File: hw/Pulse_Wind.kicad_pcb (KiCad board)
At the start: 2 copper layers, 14 x 21 mm, 22 parts, among them J1 AudioJack4, J2 Conn_01x04, U1 PY32F003F18U6, U2 SC7A20, U3 FM8002A, U4 ME6206A33XG

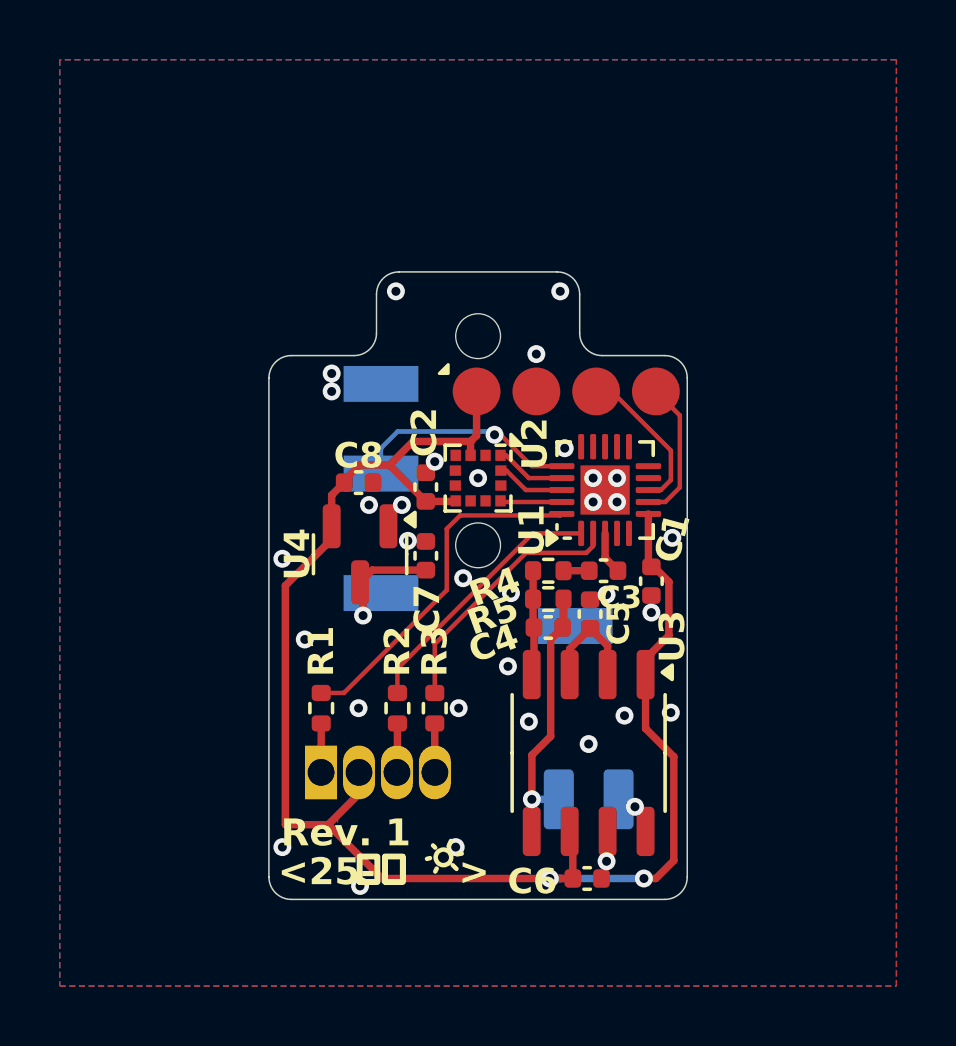
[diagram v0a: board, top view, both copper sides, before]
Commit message: hw: Fix errors (> <)
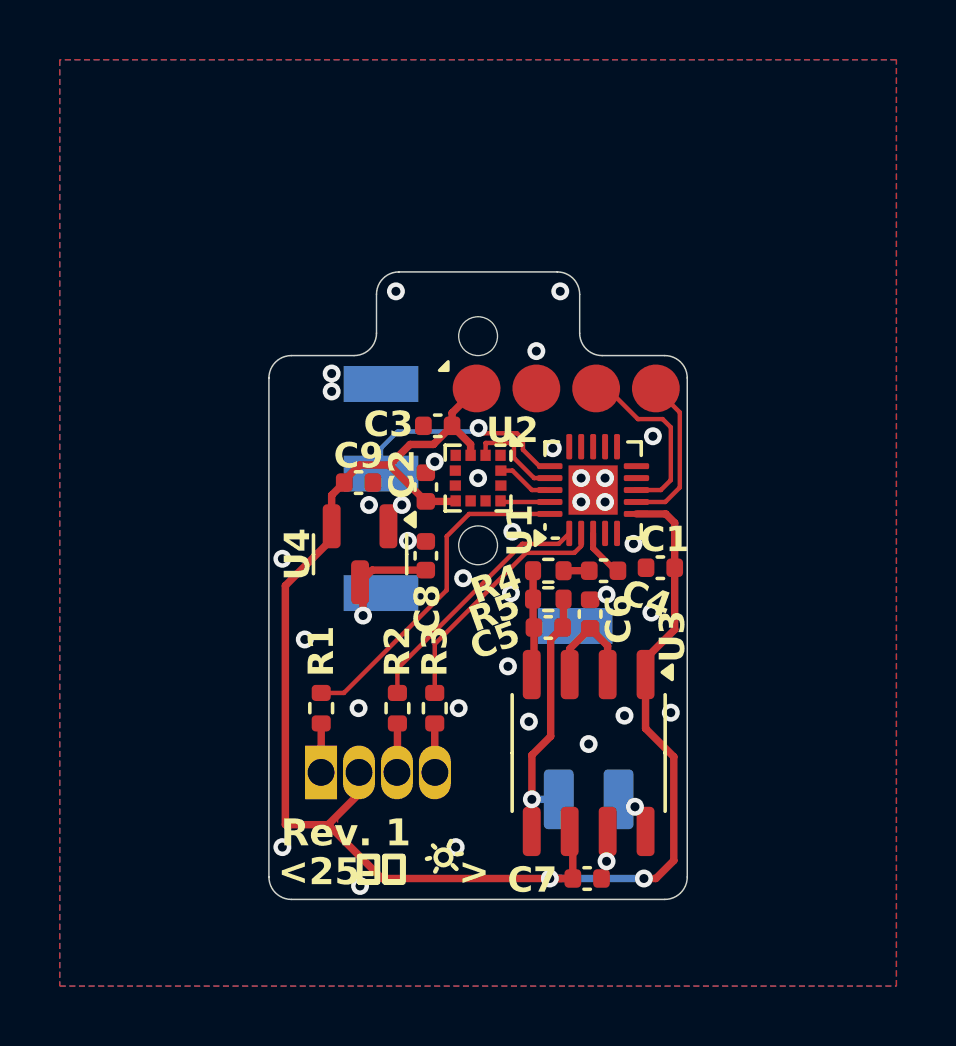
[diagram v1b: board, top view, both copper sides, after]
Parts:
- added C3: 100n, Capacitor_SMD:C_0402_1005Metric, F.Cu at (78.7, 78.2)
- moved C1 0.54 mm to (86.1, 83.0), turned to 0 degrees
- moved U1 0.40 mm to (83.8, 80.4)
- moved J2 0.10 mm to (83.0, 77.0)
- renumbered C3 to C4, C4 to C5, C5 to C6, C6 to C7, C7 to C8, C8 to C9
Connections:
- U2 pad 1: /IMU_SDA -> unconnected-(U2-SDO-Pad1)
- U2 pad 2: unconnected-(U2-SDx-Pad2) -> /IMU_SDA
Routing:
- net +3V3: track 53.7 -> 54.7 mm
- net /SWCLK: track 5.20 -> 6.19 mm
- net /IMU_SDA: track 2.37 -> 3.24 mm
- net /SWDIO: track 4.80 -> 5.40 mm
- net /LED_R: track 11.7 -> 11.2 mm
- net /IMU_SCK: track 2.31 -> 1.81 mm
- net GND: vias 33 -> 35

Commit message: hw: Connect SC7A20 NC (pin 4) to GND?
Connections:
- U2 pad 4: unconnected-(U2-NC-Pad4) -> GND
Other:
- board text added: "Rev. 1a"
- board text removed: "Rev. 1"
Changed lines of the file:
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@@
 	(net 32 "unconnected-(U2-INT2-Pad6)")
 	(net 33 "unconnected-(U2-INT1-Pad5)")
-	(net 34 "unconnected-(U2-NC-Pad4)")
-	(net 35 "unconnected-(U2-SDO-Pad1)")
+	(net 34 "unconnected-(U2-SDO-Pad1)")
 	(footprint "Capacitor_SMD:C_0402_1005Metric"
 		(layer "F.Cu")
@@
 			(size 0.375 0.35)
 			(layers "F.Cu" "F.Mask" "F.Paste")
-			(net 35 "unconnected-(U2-SDO-Pad1)")
+			(net 34 "unconnected-(U2-SDO-Pad1)")
 			(pinfunction "SDO")
 			(pintype "bidirectional+no_connect")
@@
 			(size 0.375 0.35)
 			(layers "F.Cu" "F.Mask" "F.Paste")
-			(net 34 "unconnected-(U2-NC-Pad4)")
+			(net 2 "GND")
 			(pinfunction "NC")
-			(pintype "passive+no_connect")
+			(pintype "passive")
 		)
 		(pad "5" smd rect
@@
 		)
 	)
-	(gr_text "Rev. 1"
+	(gr_text "Rev. 1a"
 		(at 73.4 92.4 0)
 		(layer "F.SilkS")
@@
 			(justify left bottom)
 		)
-		(render_cache "Rev. 1" 0
+		(render_cache "Rev. 1a" 0
 			(polygon
 				(pts
@@
 				)
 			)
+			(polygon
+				(pts
+					(xy 77.093753 91.625692) (xy 77.156814 91.641513) (xy 77.207073 91.667072) (xy 77.246516 91.702132)
+					(xy 77.262657 91.723709) (xy 77.276069 91.747732) (xy 77.287187 91.775525) (xy 77.295269 91.805943)
+					(xy 77.300519 91.841223) (xy 77.302274 91.879408) (xy 77.302274 92.247) (xy 77.186319 92.247) (xy 77.163678 92.188033)
+					(xy 77.147202 92.203342) (xy 77.12421 92.220312) (xy 77.099084 92.234398) (xy 77.071159 92.245821)
+					(xy 77.041216 92.254104) (xy 77.008242 92.259318) (xy 76.97337 92.261068) (xy 76.913479 92.255402)
+					(xy 76.860479 92.238137) (xy 76.818729 92.211013) (xy 76.788002 92.175036) (xy 76.776798 92.153738)
+					(xy 76.768609 92.130453) (xy 76.763478 92.104718) (xy 76.76174 92.077135) (xy 76.763138 92.056417)
+					(xy 76.922977 92.056417) (xy 76.928621 92.08465) (xy 76.936637 92.098503) (xy 76.947826 92.110422)
+					(xy 76.962842 92.120714) (xy 76.98084 92.128408) (xy 77.002288 92.133395) (xy 77.026291 92.135112)
+					(xy 77.056375 92.132731) (xy 77.080763 92.126975) (xy 77.103399 92.118018) (xy 77.12453 92.105802)
+					(xy 77.14351 92.090709) (xy 77.14351 91.972666) (xy 77.053536 91.977691) (xy 76.988031 91.98988)
+					(xy 76.950524 92.00653) (xy 76.930236 92.027459) (xy 76.924763 92.041108) (xy 76.922977 92.056417)
+					(xy 76.763138 92.056417) (xy 76.763543 92.050418) (xy 76.776166 92.007284) (xy 76.787234 91.988046)
+					(xy 76.801518 91.9705) (xy 76.820361 91.953619) (xy 76.842984 91.938613) (xy 76.872512 91.924159)
+					(xy 76.906833 91.911939) (xy 76.951464 91.90078) (xy 77.002436 91.892377) (xy 77.068657 91.886082)
+					(xy 77.14351 91.883255) (xy 77.14351 91.866658) (xy 77.140618 91.838607) (xy 77.126546 91.805323)
+					(xy 77.114725 91.791293) (xy 77.099878 91.779503) (xy 77.080144 91.769156) (xy 77.056878 91.761548)
+					(xy 77.026709 91.756305) (xy 76.992274 91.754551) (xy 76.979241 91.754774) (xy 76.940063 91.758016)
+					(xy 76.899731 91.765117) (xy 76.855935 91.776787) (xy 76.810869 91.792744) (xy 76.77306 91.680197)
+					(xy 76.809858 91.663036) (xy 76.849481 91.648616) (xy 76.893389 91.636543) (xy 76.938645 91.627807)
+					(xy 77.026291 91.620956)
+				)
+			)
 		)
 	)
@@
 	)
 	(gr_text "JLCJLCJLCJLC"
-		(at 73.35 76.2 270)
+		(at 81.85 73.7 270)
 		(layer "B.SilkS")
 		(effects
